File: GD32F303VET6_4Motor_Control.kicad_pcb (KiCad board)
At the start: 6 copper layers, 100 x 60 mm, 173 parts, among them CN1 KF128L-5.08-2P, CN4 WJ15EDGRC-3.81-2P, CN5 KF15EDGRC3.81-6P, CN6 KF15EDGRC3.81-6P, CN7 KF15EDGRC3.81-6P, CN8 KF15EDGRC3.81-6P, J1 TYPE-C-31-M-31, J2 TYPE-C 16PIN 2MD(073), Q10 CJ3134K, Q11 CJ3134K, Q12 CJ3134K, Q13 CJ3134K, Q14 CJ3134K, Q15 CJ3134K, Q16 CJ3134K KF, Q17 CJ3134K KF, Q3 CJ3134K, Q4 CJ3134K, Q5 CJ3134K, Q6 CJ3134K, Q7 CJ3134K, Q8 CJ3134K, Q9 CJ3134K, SW1 SKRPACE010, U1 XL1509-5.0, U13 SIT3485ESA, U15 TXS0104EPWR, U19 CH340N, U20 LM66100DCKR, U21 LM66100DCKR, U5 LM66100DCKR, U6 SY8089A1AAC, U7 GD32F303VET6, U8 GD25Q16ESIGR, Y1 TAXM8M4RDBCCT2T, Y2 XKXGI-SUA-32.768K

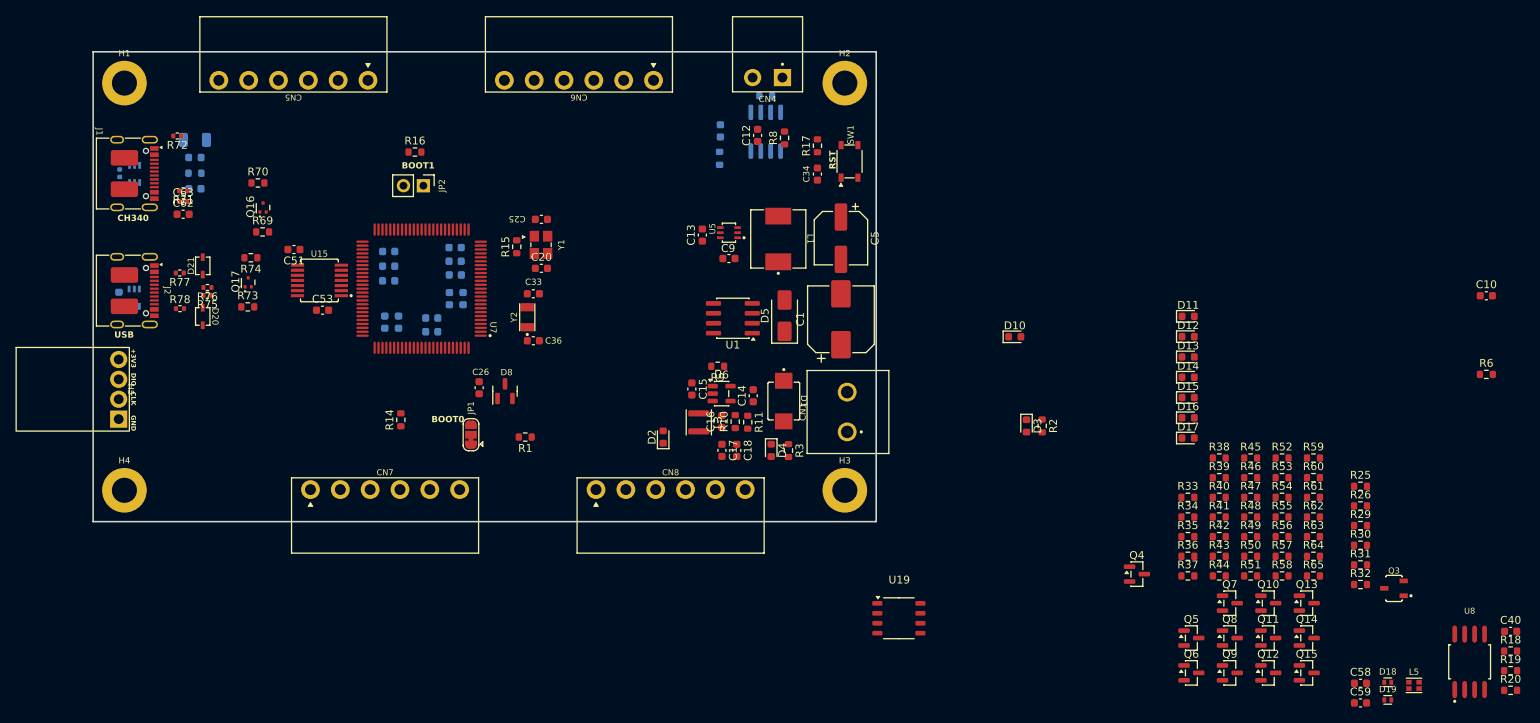
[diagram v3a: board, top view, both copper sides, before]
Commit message: V2.0: update motor control schematics, replicated PCB layout and component libraries
Save current KiCad design progress, including four motor control layouts and new component libraries. PCB routing and DRC cleanup remain unfinished; this is not a fabrication release.
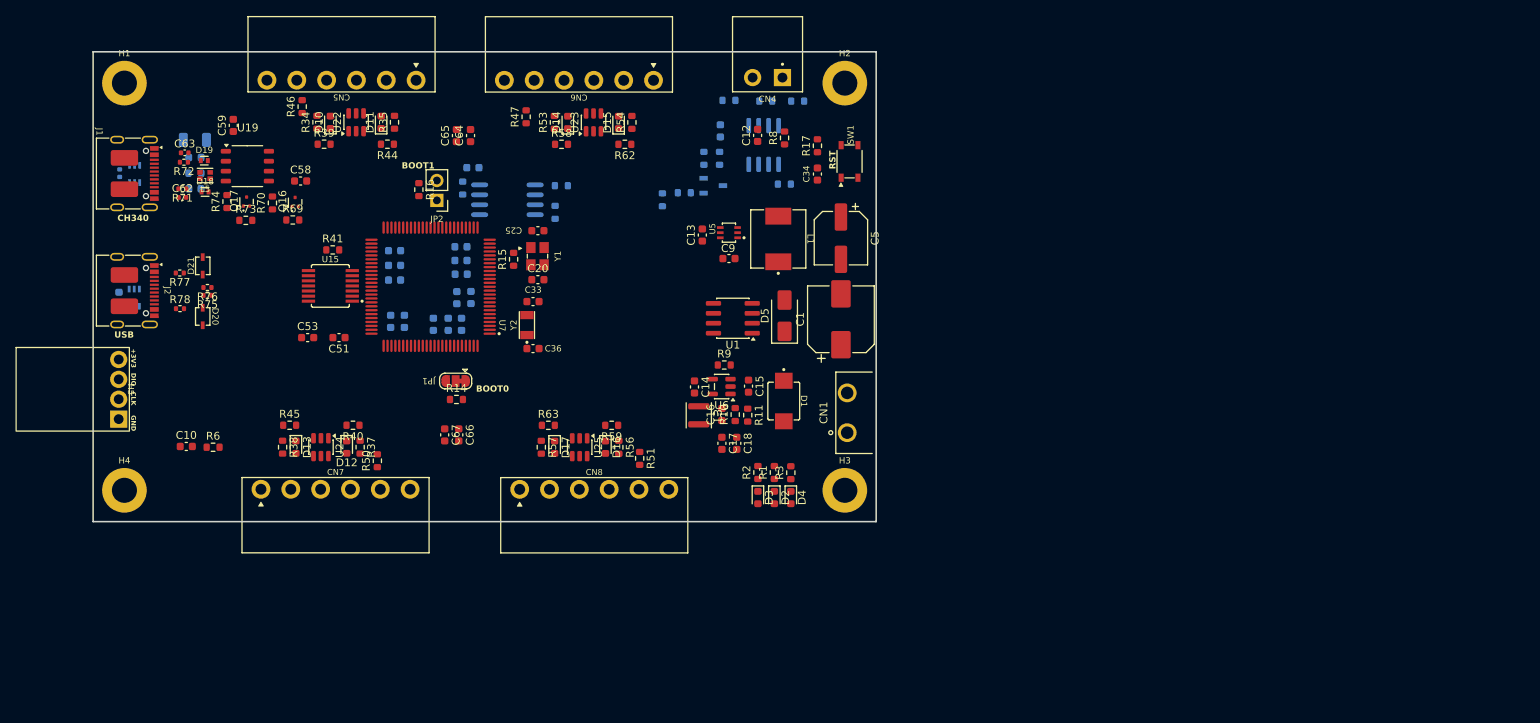
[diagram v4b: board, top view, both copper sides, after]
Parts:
- removed D8: BAT54CTA, kicad_api_lib:BAT54CTA
- removed Q10, Q11, Q12, Q13, Q14, Q15, Q4, Q5, Q6, Q7, Q8, Q9: CJ3134K, Package_TO_SOT_SMD:SOT-23
- removed R33, R36, R42, R43, R52, R55, R60, R61: 100, Resistor_SMD:R_0603_1608Metric
- removed R48, R49, R64, R65: 10k, Resistor_SMD:R_0603_1608Metric
- added C64: 100nF, Capacitor_SMD:C_0603_1608Metric, F.Cu at (133.7, 69.7)
- added C65: 100nF, Capacitor_SMD:C_0603_1608Metric, F.Cu at (131.9, 69.7)
- added C66: 100nF, Capacitor_SMD:C_0603_1608Metric, F.Cu at (132.2, 107.9)
- added C67: 100nF, Capacitor_SMD:C_0603_1608Metric, F.Cu at (130.4, 107.9)
- added U22: SN74LVC2G06DBVR, Package_TO_SOT_SMD:SOT-23-6, F.Cu at (119.1, 68.0)
- added U23: SN74LVC2G06DBVR, Package_TO_SOT_SMD:SOT-23-6, F.Cu at (149.4, 68.0)
- added U24: SN74LVC2G06DBVR, Package_TO_SOT_SMD:SOT-23-6, F.Cu at (114.6, 109.5)
- added U25: SN74LVC2G06DBVR, Package_TO_SOT_SMD:SOT-23-6, F.Cu at (147.6, 109.5)
- C26, C40, Q3, R18, R19, R20, R25, R26, R29, R30, R31, R32, U8: moved to B.Cu
- C62: footprint Capacitor_SMD:C_0603_1608Metric -> Capacitor_SMD:C_0402_1005Metric
- CN1: value KF128L-5.08-2P -> KF2EDGK-5.08-2P; footprint kicad_api_lib:KF128L-5.08-2P -> kicad_api_lib:KF2EDGR-5.08-2P
- R35, R38, R54, R57: value 1k -> 2.2k
- moved L5 167.6 mm to (99.8, 74.8), turned to 180 degrees
- moved C10 167.1 mm to (97.4, 109.4)
- moved D19 166.1 mm to (99.7, 72.9)
- moved D18 163.5 mm to (99.8, 76.9)
- moved R6 162.9 mm to (100.8, 109.5)
- moved C59 161.7 mm to (103.4, 68.4), turned to 90 degrees
- moved C58 149.8 mm to (112.0, 75.5)
- moved R20 148.4 mm to (132.7, 76.4), turned to -90 degrees
- moved C40 145.2 mm to (134.0, 73.8)
- moved U8 136.3 mm to (138.4, 77.9), turned to -90 degrees
- moved R19 135.3 mm to (144.5, 79.5), turned to 90 degrees
- moved R18 135.0 mm to (145.3, 76.1)
- moved R46 130.1 mm to (112.2, 66.0), turned to 90 degrees
- moved R45 122.8 mm to (110.6, 106.7)
- moved R34 122.1 mm to (114.1, 68.0), turned to 90 degrees
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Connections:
- C26 pad 1: Net-(U7A-VBAT) -> +3V3
- D11 pad 1: GND -> /MCU_Core/BRAKE1_1
- D13 pad 1: GND -> /MCU_Core/BRAKE1_3
- D15 pad 1: GND -> /MCU_Core/BRAKE1_2
- D17 pad 1: GND -> /MCU_Core/BRAKE1_4
- D4 pad 1: GND -> Net-(D4-K)
- D4 pad 2: Net-(D4-A) -> +24V
- L5 pad 1: /MCU_Core/USB_TTL_CH340/DN -> Net-(U19-UD+)
- L5 pad 2: Net-(U19-UD-) -> /MCU_Core/USB_TTL_CH340/DP
- L5 pad 3: Net-(U19-UD+) -> /MCU_Core/USB_TTL_CH340/DN
- L5 pad 4: /MCU_Core/USB_TTL_CH340/DP -> Net-(U19-UD-)
- R3 pad 1: +24V -> Net-(D4-K)
- R3 pad 2: Net-(D4-A) -> GND
- R35 pad 1: /MCU_Core/BRAKE1_1 -> +3V3
- R38 pad 1: /MCU_Core/BRAKE1_3 -> +3V3
- R39 pad 1: Net-(Q4-G) -> /MCU_Core/DIR1_1
- R40 pad 1: Net-(Q5-G) -> /MCU_Core/DIR1_3
- R44 pad 1: Net-(Q6-G) -> +3V3
- R44 pad 2: GND -> /MCU_Core/BRAKE1_1
- R45 pad 1: Net-(Q7-G) -> +3V3
- R45 pad 2: GND -> /MCU_Core/BRAKE1_3
- R54 pad 1: /MCU_Core/BRAKE1_2 -> +3V3
- R57 pad 1: /MCU_Core/BRAKE1_4 -> +3V3
- R58 pad 1: Net-(Q10-G) -> /MCU_Core/DIR1_2
- R59 pad 1: Net-(Q11-G) -> /MCU_Core/DIR1_4
- R62 pad 1: Net-(Q12-G) -> +3V3
- R62 pad 2: GND -> /MCU_Core/BRAKE1_2
- R63 pad 1: Net-(Q13-G) -> +3V3
- R63 pad 2: GND -> /MCU_Core/BRAKE1_4
- U7 pad 29: unconnected-(U7E-PA4/SPI0_NSS/USART1_CK/ADC01_IN4/DAC_OUT-Pad29) -> /MCU_Core/MCU_SPI_NSS
- U7 pad 30: unconnected-(U7E-PA5/SPI0_SCK/ADC01_IN5/DAC0_OUT1-Pad30) -> /MCU_Core/MCU_SPI_SLK
- U7 pad 31: unconnected-(U7E-PA6/SPI0_MISO/ADC01_IN6/TIMER2_CH0/TIMER7_BRKIN-Pad31) -> /MCU_Core/MCU_SPI_MISO
- U7 pad 32: /MCU_Core/BRAKE1_2 -> /MCU_Core/MCU_SPI_MOSI
- U7 pad 33: unconnected-(U7E-PC4/ADC01_IN14-Pad33) -> /MCU_Core/BRAKE1_2
- U7 pad 51: /MCU_Core/MCU_SPI_NSS -> unconnected-(U7E-PB12/SPI1_NSS/I2C1_SMBA/USART2_CK/TIMER0_BRKIN/I2S1_WS-Pad51)
- U7 pad 52: /MCU_Core/MCU_SPI_SLK -> unconnected-(U7E-PB13/SPI1_SCK/USART2_CTS/TIMER0_CH0_ON/I2S1_CK-Pad52)
- U7 pad 53: /MCU_Core/MCU_SPI_MISO -> unconnected-(U7E-PB14/SPI1_MISO/USART2_RTS/TIMER0_CH1_ON-Pad53)
- U7 pad 54: /MCU_Core/MCU_SPI_MOSI -> unconnected-(U7E-PB15/SPI1_MOSI/TIMER0_CH2_ON/I2S1_SD-Pad54)
- U7 pad 6: Net-(U7A-VBAT) -> +3V3

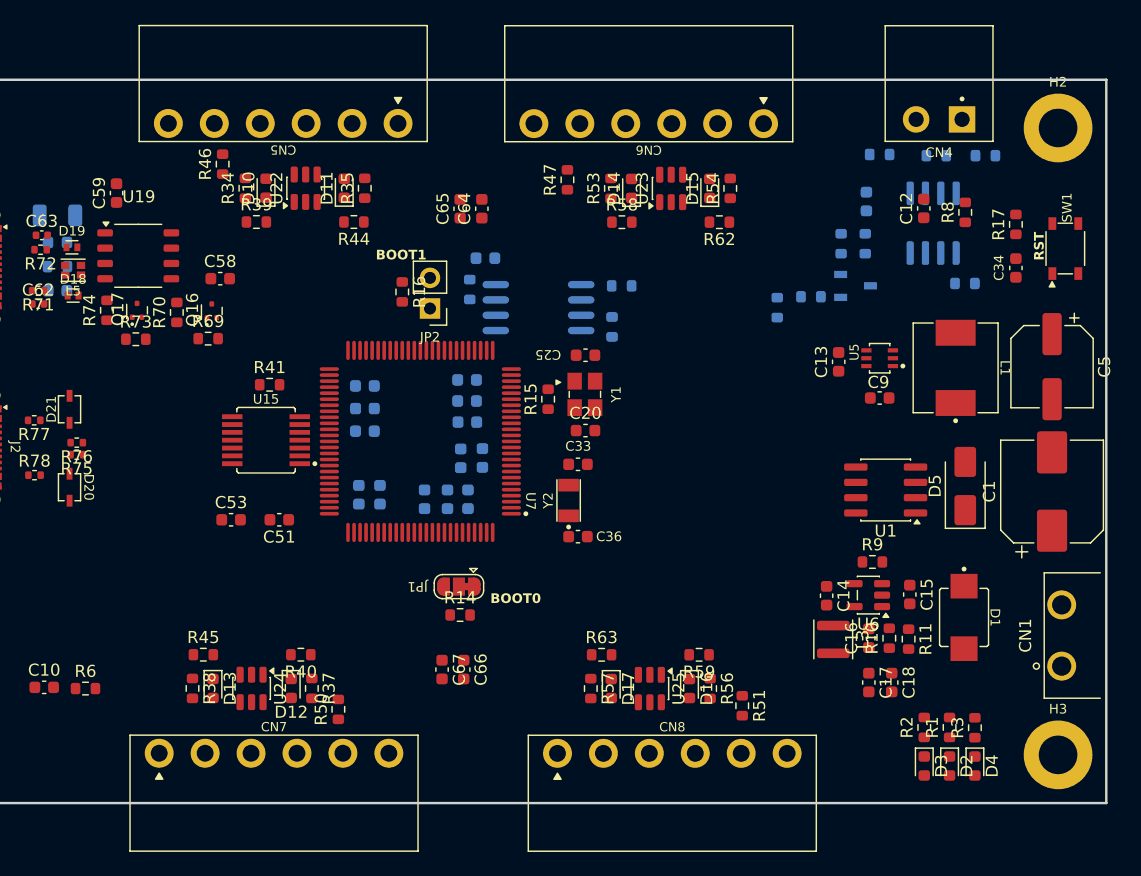
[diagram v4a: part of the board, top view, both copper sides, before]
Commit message: V2.0: add minimal ESP32-C3 Wi-Fi OTA hardware and save current PCB layout
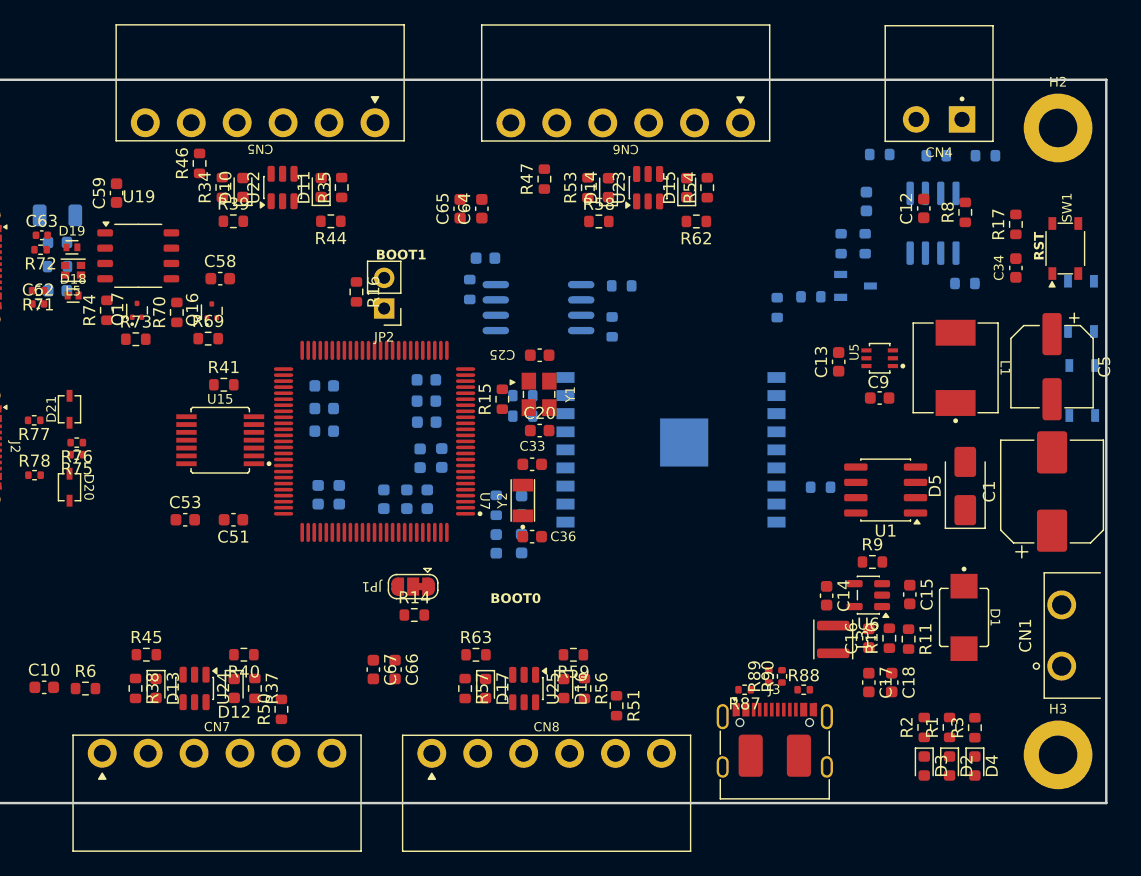
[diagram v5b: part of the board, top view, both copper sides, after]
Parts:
- added C68: 10uF / 10V X5R, Capacitor_SMD:C_0603_1608Metric, B.Cu at (137.0, 97.5)
- added C69: 100nF / 16V X7R, Capacitor_SMD:C_0603_1608Metric, B.Cu at (134.9, 97.5)
- added C70: 1uF / 10V, Capacitor_SMD:C_0603_1608Metric, B.Cu at (137.0, 94.3)
- added J3: TYPE-C-31-M-31, kicad_api_lib:TYPE-C-31-M-31, F.Cu at (158.0, 112.3)
- added R79: 10k, Resistor_SMD:R_0603_1608Metric, B.Cu at (134.9, 94.3)
- added R80: 10k, Resistor_SMD:R_0603_1608Metric, B.Cu at (161.8, 92.8)
- added R81: 10k, Resistor_SMD:R_0603_1608Metric, B.Cu at (137.1, 86.9)
- added R82: 10k, Resistor_SMD:R_0603_1608Metric, B.Cu at (137.1, 85.2)
- added R87: 5.1k 1%, Resistor_SMD:R_0402_1005Metric, F.Cu at (155.5, 109.6)
- added R88: 5.1k 1%, Resistor_SMD:R_0402_1005Metric, F.Cu at (160.4, 109.6)
- added R89: 22R, Resistor_SMD:R_0402_1005Metric, F.Cu at (157.5, 108.5)
- added R90: 22R, Resistor_SMD:R_0402_1005Metric, F.Cu at (158.6, 108.5)
- added SW2: RESET, kicad_api_lib:SKRPACE010, B.Cu at (183.4, 77.8)
- added SW3: BOOT, kicad_api_lib:SKRPACE010, B.Cu at (183.5, 84.8)
- added U26: ESP32-C3-WROOM-02-N4, kicad_api_lib:ESP32-C3-WROOM-02-N4, B.Cu at (149.4, 92.8)
- moved CN8 10.4 mm to (139.1, 114.9)
- moved D16 10.4 mm to (140.5, 109.5)
- moved D17 10.4 mm to (134.0, 109.5)
- moved R51 10.4 mm to (144.9, 110.9)
- moved R57 10.4 mm to (132.3, 109.5)
- moved R56 10.4 mm to (142.2, 109.5)
- moved R59 10.4 mm to (141.3, 106.7)
- moved R63 10.4 mm to (133.2, 106.7)
- moved U25 10.4 mm to (137.2, 109.5)
- moved C67 5.70 mm to (124.7, 107.9)
- moved C66 5.70 mm to (126.5, 107.9)
- moved CN7 4.73 mm to (111.7, 114.9)
- moved D12 4.73 mm to (113.2, 109.5)
- moved D13 4.73 mm to (106.7, 109.5)
- moved R38 4.73 mm to (105.0, 109.5)
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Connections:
- U7 pad 55: unconnected-(U7E-PD8/EXMC_D13-Pad55) -> /MCU_Core/WIFI_TX
- U7 pad 56: unconnected-(U7E-PD9/EXMC_D14-Pad56) -> /MCU_Core/WIFI_RX

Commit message: 停用 WiFi OTA 装配并从 PCB 排除
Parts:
- removed C68: 10uF / 10V X5R, Capacitor_SMD:C_0603_1608Metric
- removed C69: 100nF / 16V X7R, Capacitor_SMD:C_0603_1608Metric
- removed C70: 1uF / 10V, Capacitor_SMD:C_0603_1608Metric
- removed J3: TYPE-C-31-M-31, kicad_api_lib:TYPE-C-31-M-31
- removed R79, R80, R81, R82: 10k, Resistor_SMD:R_0603_1608Metric
- removed R87, R88: 5.1k 1%, Resistor_SMD:R_0402_1005Metric
- removed R89, R90: 22R, Resistor_SMD:R_0402_1005Metric
- removed SW2: RESET, kicad_api_lib:SKRPACE010
- removed SW3: BOOT, kicad_api_lib:SKRPACE010
- removed U26: ESP32-C3-WROOM-02-N4, kicad_api_lib:ESP32-C3-WROOM-02-N4
